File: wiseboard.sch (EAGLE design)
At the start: 91 parts, among them IC1 MCP73871-2CCI/ML-ND, IC2 LM358MX, Q1 IRLML6402TRPBF, Q2 IRLML6402TRPBF, U1 LT1945EMSPBF, X1 1528-1438-ND

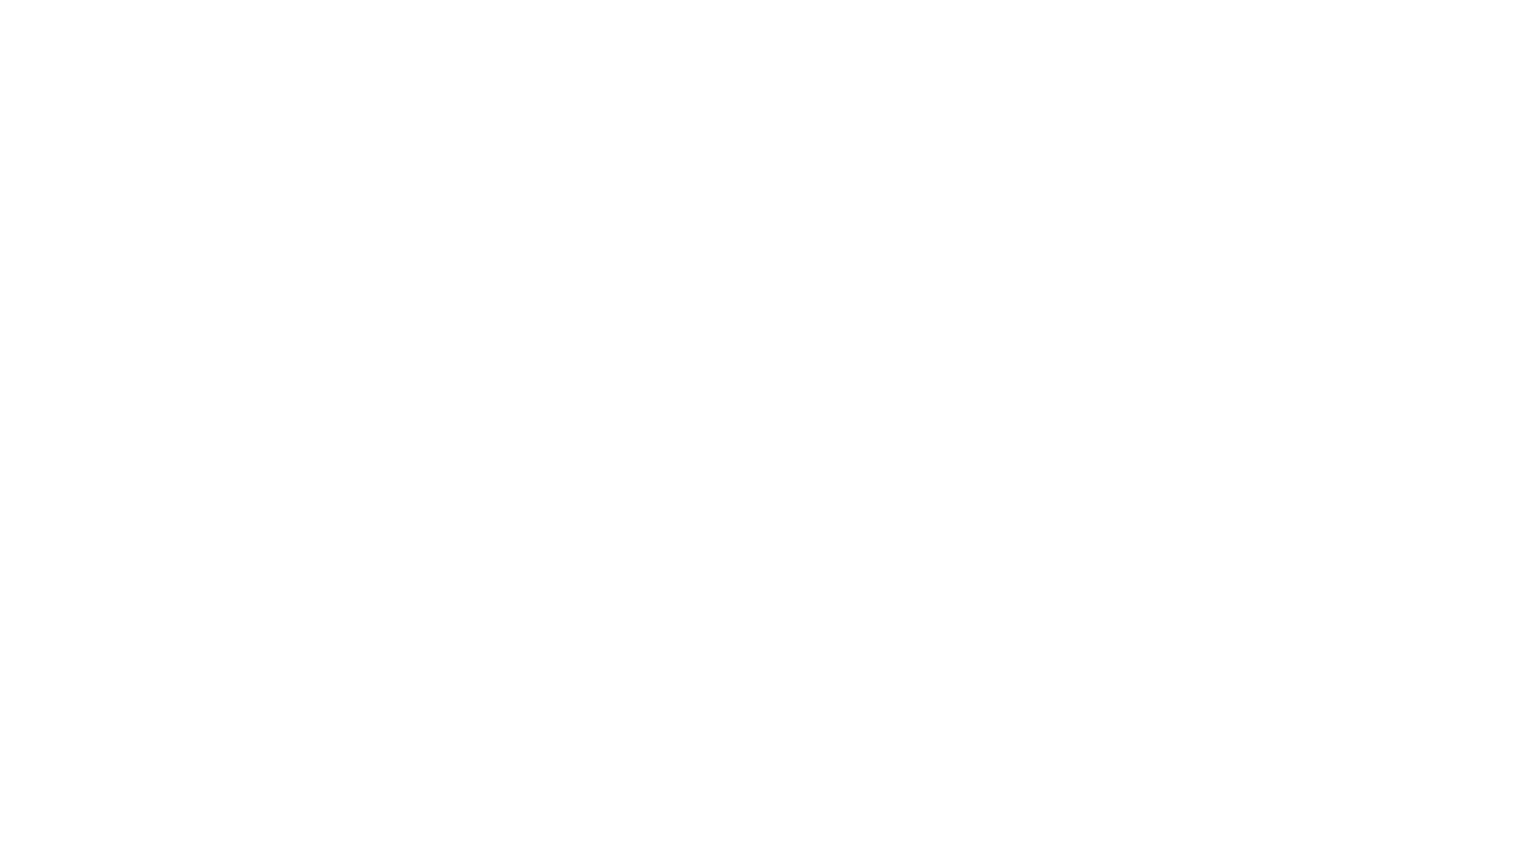
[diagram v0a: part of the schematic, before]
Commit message: ADD NEW POWER SUPPLY CHIP AND UPDATED WISE LIB
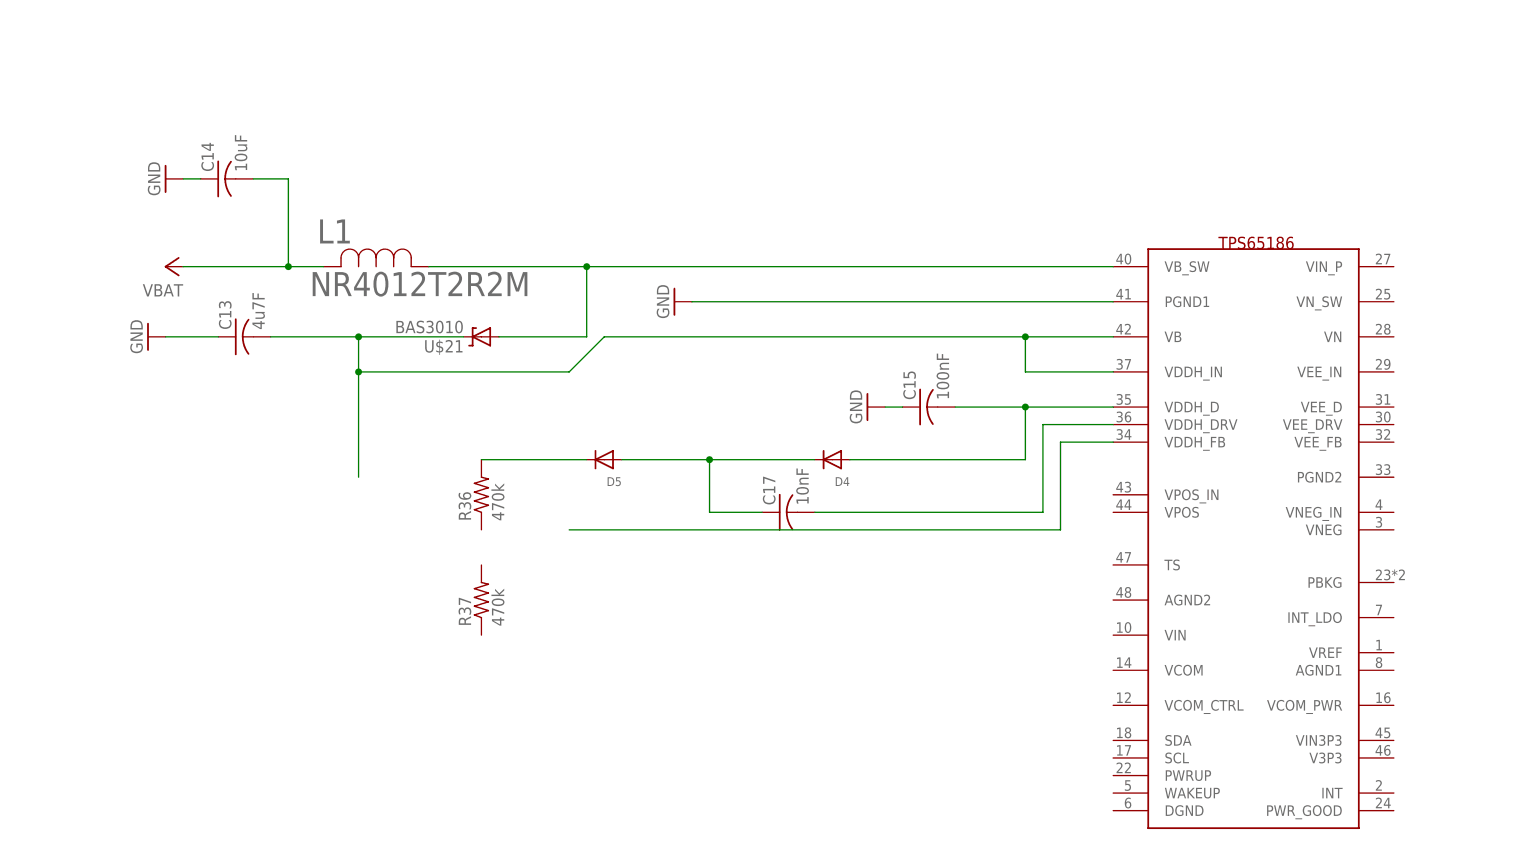
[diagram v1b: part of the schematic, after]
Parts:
- added C13: 4u7F, adafruit:C-USC1206
- added C14: 10uF, adafruit:C-USC1210
- added C15: 100nF, adafruit:C-USC1206
- added C17: 10nF, adafruit:C-USC1206
- added D4, D5: (no value), adafruit:DIODESOD-323F
- added L1: NR4012T2R2M, WISE:NR4012T2R2M
- added R36, R37: 470k, adafruit:R-US_M1206
- added U$20: TPS65186, WISE:TPS65186
- added U$21: BAS3010, WISE:DIODE-ZENER-BZT52
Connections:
- new net N$17: L1.2, U$20.VB_SW, U$21.A
- new net N$28: C13.2, U$20.VB, U$20.VDDH_IN, U$21.C
- new net N$30: C15.2, D4.A, U$20.VDDH_D
- new net N$32: C17.1, D4.C, D5.A
- new net N$34: C17.2, U$20.VDDH_DRV
- new net N$36: D5.C, R36.2
- new net N$37: U$20.VDDH_FB
- net GND: now also C13.1, C14.1, C15.1, U$20.PGND1
- net VBAT: now also C14.2, L1.1
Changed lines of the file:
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@@
 <part name="CN1" library="adafruit" deviceset="JST_2PIN" device="-SMT-RA"/>
 <part name="GND16" library="supply1" library_urn="urn:adsk.eagle:library:371" deviceset="GND" device=""/>
+<part name="U$20" library="WISE" deviceset="TPS65186" device=""/>
+<part name="C13" library="adafruit" deviceset="C-US" device="C1206" value="4u7F"/>
+<part name="C14" library="adafruit" deviceset="C-US" device="C1210" value="10uF"/>
+<part name="L1" library="WISE" deviceset="NR4012T2R2M" device=""/>
+<part name="U$21" library="WISE" deviceset="DIODE-ZENER" device="-BZT52" value="BAS3010"/>
+<part name="GND47" library="supply1" library_urn="urn:adsk.eagle:library:371" deviceset="GND" device=""/>
+<part name="VBAT4" library="supply1" library_urn="urn:adsk.eagle:library:371" deviceset="VBAT" device=""/>
+<part name="GND48" library="supply1" library_urn="urn:adsk.eagle:library:371" deviceset="GND" device=""/>
+<part name="GND49" library="supply1" library_urn="urn:adsk.eagle:library:371" deviceset="GND" device=""/>
+<part name="C15" library="adafruit" deviceset="C-US" device="C1206" value="100nF"/>
+<part name="GND50" library="supply1" library_urn="urn:adsk.eagle:library:371" deviceset="GND" device=""/>
+<part name="D4" library="adafruit" deviceset="DIODE" device="SOD-323F"/>
+<part name="C17" library="adafruit" deviceset="C-US" device="C1206" value="10nF"/>
+<part name="D5" library="adafruit" deviceset="DIODE" device="SOD-323F"/>
+<part name="R36" library="adafruit" deviceset="R-US_" device="M1206" value="470k"/>
+<part name="R37" library="adafruit" deviceset="R-US_" device="M1206" value="470k"/>
 </parts>
 <sheets>
@@
 <instance part="CN1" gate="G$1" x="375.92" y="-154.94"/>
 <instance part="GND16" gate="1" x="360.68" y="-152.4" rot="R270"/>
+<instance part="U$20" gate="G$1" x="-203.2" y="-251.46"/>
+<instance part="C13" gate="G$1" x="-360.68" y="-220.98" rot="R90"/>
+<instance part="C14" gate="G$1" x="-363.22" y="-198.12" rot="R90"/>
+<instance part="L1" gate="A" x="-347.98" y="-210.82"/>
+<instance part="U$21" gate="G$1" x="-325.12" y="-220.98" rot="R180"/>
+<instance part="GND47" gate="1" x="-373.38" y="-220.98" rot="R270"/>
+<instance part="VBAT4" gate="G$1" x="-370.84" y="-210.82" rot="R90"/>
+<instance part="GND48" gate="1" x="-370.84" y="-198.12" rot="R270"/>
+<instance part="GND49" gate="1" x="-297.18" y="-215.9" rot="R270"/>
+<instance part="C15" gate="G$1" x="-261.62" y="-231.14" rot="R90"/>
+<instance part="GND50" gate="1" x="-269.24" y="-231.14" rot="R270"/>
+<instance part="D4" gate="G$1" x="-274.32" y="-238.76" rot="R180"/>
+<instance part="C17" gate="G$1" x="-281.94" y="-246.38" rot="R90"/>
+<instance part="D5" gate="G$1" x="-307.34" y="-238.76" rot="R180"/>
+<instance part="R36" gate="G$1" x="-325.12" y="-243.84" rot="R90"/>
+<instance part="R37" gate="G$1" x="-325.12" y="-259.08" rot="R90"/>
 </instances>
 <busses>
@@
 <wire x1="373.38" y1="-152.4" x2="363.22" y2="-152.4" width="0.1524" layer="91"/>
 <pinref part="GND16" gate="1" pin="GND"/>
+</segment>
+<segment>
+<pinref part="C13" gate="G$1" pin="1"/>
+<pinref part="GND47" gate="1" pin="GND"/>
+<wire x1="-370.84" y1="-220.98" x2="-363.22" y2="-220.98" width="0.1524" layer="91"/>
+</segment>
+<segment>
+<pinref part="C14" gate="G$1" pin="1"/>
+<wire x1="-365.76" y1="-198.12" x2="-368.3" y2="-198.12" width="0.1524" layer="91"/>
+<pinref part="GND48" gate="1" pin="GND"/>
+</segment>
+<segment>
+<pinref part="U$20" gate="G$1" pin="PGND1"/>
+<pinref part="GND49" gate="1" pin="GND"/>
+<wire x1="-294.64" y1="-215.9" x2="-233.68" y2="-215.9" width="0.1524" layer="91"/>
+</segment>
+<segment>
+<pinref part="C15" gate="G$1" pin="1"/>
+<pinref part="GND50" gate="1" pin="GND"/>
+<wire x1="-266.7" y1="-231.14" x2="-264.16" y2="-231.14" width="0.1524" layer="91"/>
 </segment>
 </net>
@@
 <wire x1="373.38" y1="-154.94" x2="353.06" y2="-154.94" width="0.1524" layer="91"/>
 <junction x="353.06" y="-154.94"/>
+</segment>
+<segment>
+<pinref part="VBAT4" gate="G$1" pin="VBAT"/>
+<pinref part="L1" gate="A" pin="1"/>
+<wire x1="-368.3" y1="-210.82" x2="-353.06" y2="-210.82" width="0.1524" layer="91"/>
+<pinref part="C14" gate="G$1" pin="2"/>
+<wire x1="-353.06" y1="-210.82" x2="-347.98" y2="-210.82" width="0.1524" layer="91"/>
+<wire x1="-358.14" y1="-198.12" x2="-353.06" y2="-198.12" width="0.1524" layer="91"/>
+<wire x1="-353.06" y1="-198.12" x2="-353.06" y2="-210.82" width="0.1524" layer="91"/>
+<junction x="-353.06" y="-210.82"/>
 </segment>
 </net>
@@
 </segment>
 </net>
+<net name="N$17" class="0">
+<segment>
+<pinref part="U$20" gate="G$1" pin="VB_SW"/>
+<pinref part="L1" gate="A" pin="2"/>
+<wire x1="-233.68" y1="-210.82" x2="-309.88" y2="-210.82" width="0.1524" layer="91"/>
+<pinref part="U$21" gate="G$1" pin="A"/>
+<wire x1="-309.88" y1="-210.82" x2="-332.74" y2="-210.82" width="0.1524" layer="91"/>
+<wire x1="-322.58" y1="-220.98" x2="-309.88" y2="-220.98" width="0.1524" layer="91"/>
+<wire x1="-309.88" y1="-220.98" x2="-309.88" y2="-210.82" width="0.1524" layer="91"/>
+<junction x="-309.88" y="-210.82"/>
+</segment>
+</net>
+<net name="N$28" class="0">
+<segment>
+<pinref part="U$21" gate="G$1" pin="C"/>
+<pinref part="C13" gate="G$1" pin="2"/>
+<wire x1="-327.66" y1="-220.98" x2="-342.9" y2="-220.98" width="0.1524" layer="91"/>
+<wire x1="-342.9" y1="-220.98" x2="-355.6" y2="-220.98" width="0.1524" layer="91"/>
+<wire x1="-342.9" y1="-220.98" x2="-342.9" y2="-226.06" width="0.1524" layer="91"/>
+<junction x="-342.9" y="-220.98"/>
+<pinref part="U$20" gate="G$1" pin="VB"/>
+<wire x1="-342.9" y1="-226.06" x2="-342.9" y2="-241.3" width="0.1524" layer="91"/>
+<wire x1="-233.68" y1="-220.98" x2="-246.38" y2="-220.98" width="0.1524" layer="91"/>
+<wire x1="-246.38" y1="-220.98" x2="-307.34" y2="-220.98" width="0.1524" layer="91"/>
+<wire x1="-307.34" y1="-220.98" x2="-312.42" y2="-226.06" width="0.1524" layer="91"/>
+<wire x1="-312.42" y1="-226.06" x2="-342.9" y2="-226.06" width="0.1524" layer="91"/>
+<junction x="-342.9" y="-226.06"/>
+<pinref part="U$20" gate="G$1" pin="VDDH_IN"/>
+<wire x1="-233.68" y1="-226.06" x2="-246.38" y2="-226.06" width="0.1524" layer="91"/>
+<wire x1="-246.38" y1="-226.06" x2="-246.38" y2="-220.98" width="0.1524" layer="91"/>
+<junction x="-246.38" y="-220.98"/>
+</segment>
+</net>
+<net name="N$30" class="0">
+<segment>
+<pinref part="U$20" gate="G$1" pin="VDDH_D"/>
+<wire x1="-233.68" y1="-231.14" x2="-246.38" y2="-231.14" width="0.1524" layer="91"/>
+<wire x1="-246.38" y1="-231.14" x2="-246.38" y2="-238.76" width="0.1524" layer="91"/>
+<wire x1="-246.38" y1="-238.76" x2="-271.78" y2="-238.76" width="0.1524" layer="91"/>
+<pinref part="C15" gate="G$1" pin="2"/>
+<wire x1="-246.38" y1="-231.14" x2="-256.54" y2="-231.14" width="0.1524" layer="91"/>
+<junction x="-246.38" y="-231.14"/>
+<pinref part="D4" gate="G$1" pin="A"/>
+</segment>
+</net>
+<net name="N$32" class="0">
+<segment>
+<pinref part="D4" gate="G$1" pin="C"/>
+<wire x1="-276.86" y1="-238.76" x2="-292.1" y2="-238.76" width="0.1524" layer="91"/>
+<pinref part="C17" gate="G$1" pin="1"/>
+<wire x1="-284.48" y1="-246.38" x2="-292.1" y2="-246.38" width="0.1524" layer="91"/>
+<wire x1="-292.1" y1="-246.38" x2="-292.1" y2="-238.76" width="0.1524" layer="91"/>
+<wire x1="-292.1" y1="-238.76" x2="-304.8" y2="-238.76" width="0.1524" layer="91"/>
+<junction x="-292.1" y="-238.76"/>
+<pinref part="D5" gate="G$1" pin="A"/>
+</segment>
+</net>
+<net name="N$34" class="0">
+<segment>
+<pinref part="U$20" gate="G$1" pin="VDDH_DRV"/>
+<wire x1="-233.68" y1="-233.68" x2="-243.84" y2="-233.68" width="0.1524" layer="91"/>
+<wire x1="-243.84" y1="-233.68" x2="-243.84" y2="-246.38" width="0.1524" layer="91"/>
+<wire x1="-243.84" y1="-246.38" x2="-276.86" y2="-246.38" width="0.1524" layer="91"/>
+<pinref part="C17" gate="G$1" pin="2"/>
+</segment>
+</net>
+<net name="N$36" class="0">
+<segment>
+<pinref part="D5" gate="G$1" pin="C"/>
+<wire x1="-309.88" y1="-238.76" x2="-325.12" y2="-238.76" width="0.1524" layer="91"/>
+<pinref part="R36" gate="G$1" pin="2"/>
+</segment>
+</net>
+<net name="N$37" class="0">
+<segment>
+<pinref part="U$20" gate="G$1" pin="VDDH_FB"/>
+<wire x1="-233.68" y1="-236.22" x2="-241.3" y2="-236.22" width="0.1524" layer="91"/>
+<wire x1="-241.3" y1="-236.22" x2="-241.3" y2="-248.92" width="0.1524" layer="91"/>
+<wire x1="-241.3" y1="-248.92" x2="-312.42" y2="-248.92" width="0.1524" layer="91"/>
+</segment>
+</net>

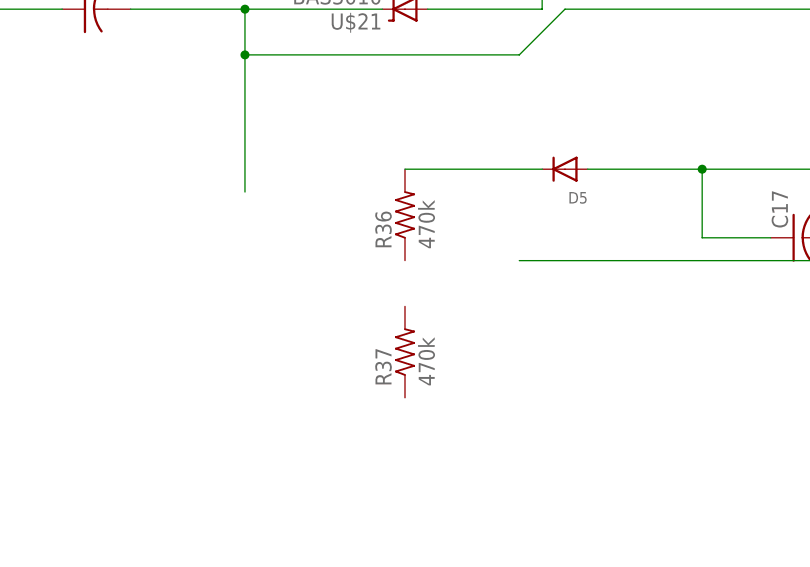
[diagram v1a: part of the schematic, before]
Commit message: CREATED BRANCH FOR TPS ALTERNATIVE POWER SOULTION
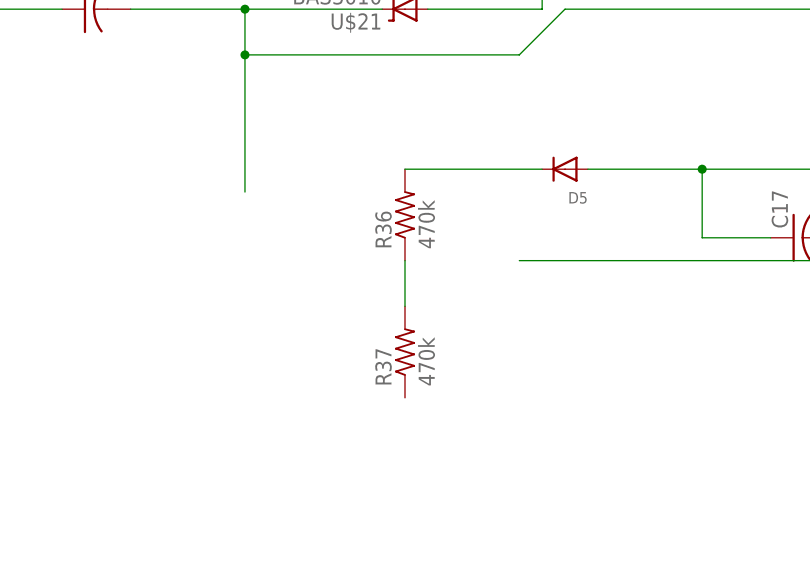
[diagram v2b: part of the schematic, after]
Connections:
- new net N$38: R36.1, R37.2
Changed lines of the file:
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@@
+</segment>
+</net>
+<net name="N$38" class="0">
+<segment>
+<pinref part="R37" gate="G$1" pin="2"/>
+<pinref part="R36" gate="G$1" pin="1"/>
+<wire x1="-325.12" y1="-254" x2="-325.12" y2="-248.92" width="0.1524" layer="91"/>
 </segment>
 </net>
